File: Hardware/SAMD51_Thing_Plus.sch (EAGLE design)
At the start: 52 parts, among them Q1 2.5A/30V, Q2 MBT3904DW1T1, U1 MCP73831, U2 ESP-WROOM-32, U3 AP2112K-3.3V, U4 FT231XS

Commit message: First commit for samd51
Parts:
- removed C16: 0.1uF, SparkFun-Capacitors:0.1UF-0603-25V-(+80/-20%)
- removed Q2: MBT3904DW1T1, esp32-thing-temp:MBT3904DW1T1
- removed R10, R17, R18, R2: 10k, SparkFun-Resistors:10KOHM-0603-1/10W-1%
- removed R13, R14: 27, SparkFun-Resistors:27OHM1/10W1%(0603)0603-RES
- removed R9: 10k, SparkFun-Resistors:10KOHM-1/10W-1%(0603)0603
- removed S2: BTN-0, SparkFun-Electromechanical:SWITCH-MOMENTARY-2SMD-4.6X2.8MM
- added C4, C8, C9: 0.1uF, SparkFun-Capacitors:0.1UF-0402-16V-10%
- added C5: 10uF, SparkFun-Capacitors:10UF-0603-6.3V-20%
- added FD3, FD4: FIDUCIALUFIDUCIAL, SparkFun-Aesthetics:FIDUCIALUFIDUCIAL
- added J4: CORTEX_DEBUG_PTH, SparkFun-Connectors:CORTEX_DEBUG_PTH
- added J5: 455-1750-1-ND, SparkFun-Connectors:CONN_03
- added L1: FB - 30Ohm, SparkFun-Passives:INDUCTOR0603
- added R1: 10k, SparkFun-Resistors:10KOHM-0603-1/10W-1%
- added Y1: 32.768kHz, SparkFun-Clocks:CRYSTAL-32.768KHZSMD-3.2X1.5
- C1: value 0.1uF -> 15pF; device SparkFun-Capacitors:0.1UF-0603-25V-5% -> SparkFun-Capacitors:15PF-0402-50V-5%
- C11, C14: device SparkFun-Capacitors:0.1UF-0603-25V-(+80/-20%) -> SparkFun-Capacitors:0.1UF-0402-16V-10%
- C12: value 47pF -> 0.1uF; device SparkFun-Capacitors:47PF-0603-50V-5% -> SparkFun-Capacitors:0.1UF-0402-16V-10%
- C13: value 47pF -> 4.7uF; device SparkFun-Capacitors:47PF-0603-50V-5% -> SparkFun-Capacitors:4.7UF0603
- C15: value 4.7uF -> 10uF; device SparkFun-Capacitors:4.7UF-6.3V-10%(0603)0603 -> SparkFun-Capacitors:10UF-0805-10V-10%
- C2: value 10uF -> 15pF; device SparkFun-Capacitors:10UF-0805-10V-10% -> SparkFun-Capacitors:15PF-0402-50V-5%
- C3: device SparkFun-Capacitors:0.1UF-0603-25V-5% -> SparkFun-Capacitors:0.1UF-0402-16V-10%
- LOGO1: value SFE_LOGO_NAME.1_INCH -> SFE_LOGO_NAME_FLAME.2_INCH; device SparkFun-Aesthetics:SFE_LOGO_NAME.1_INCH -> SparkFun-Aesthetics:SFE_LOGO_NAME_FLAME.2_INCH
- U2: value ESP-WROOM-32 -> ATSAMD51J20A-A; device SparkFun-RF:ESP-WROOM-32 -> SparkFun-IC-Microcontroller:ATSAMD51J20A-A
- U4: value FT231XS -> RFM69HW; device SparkFun-DigitalIC:FT231XS -> SparkFun-RF:RFM69HW
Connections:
- removed net 3.3V_F: C16.1, U4.!RESET, U4.3V3OUT, U4.VCCIO
- removed net CHIP_PU: C3.1, J1.6, Q2Q1.C, R2.1, S1.2, U2.EN
- removed net DTR: Q2Q2.E, R17.1, U4.!DTR
- removed net N$10: Q2Q1.B, R17.2
- removed net N$12: Q2Q2.B, R18.2
- removed net N$7: R13.2, U4.USBDM
- removed net N$8: R14.2, U4.USBDP
- removed net RTS: Q2Q1.E, R18.1, U4.!RTS
- new net !RESET: J1.6, J4.!RESET, R1.1, S1.2, U2.!RESET
- new net N$4: J5.2, U4.ANT
- new net RFM_MISO: U2.PA19, U4.MISO
- new net RFM_MOSI: U2.PA16, U4.MOSI
- new net RFM_RESET: U2.PA20, U4.RESET
- new net RFM_SCK: U2.PA17, U4.SCK
- new net RFM_SS: U2.PA18, U4.NSS
- new net SWDCLK: J4.SWDCLK/TCK, U2.PA30
- new net SWDIO: J4.SWDIO/TMS, U2.PA31
- new net VCC: C13.1, C14.1, U2.VDDCORE
- new net VDDA: C12.1, C15.1, L1.2, U2.PA03, U2.VDDANA
- new net XIN32: C1.1, U2.PA00, Y1.1
- new net XOUT32: C2.1, U2.PA01, Y1.2
- net 0: now also U2.PA13; no longer Q2Q2.C, R9.1, S2.2, U2.IO0
- net 12: now also U2.PA07; no longer R10.2, U2.IO12
- net 13: now also U2.PA10; no longer U2.IO13
- net 14: now also U2.PA06; no longer U2.IO14
- net 15: now also U2.PA11; no longer U2.IO15
- net 16: now also U2.PA09; no longer U2.IO16
- net 17: now also U2.PA08; no longer U2.IO17
- net 18: now also U2.PB13; no longer U2.IO18
- net 19: now also U2.PB15; no longer U2.IO19
- net 2: now also U2.PB14; no longer U2.IO2
- net 20: now also U2.PA12; no longer U2.IO20
- net 21: now also U2.PB16; no longer U2.IO21
- net 22: now also U2.PB17; no longer U2.IO22
- net 23: now also U2.PB12; no longer U2.IO23
- net 25: now also U2.PA02; no longer U2.IO25
- net 26: now also U2.PA05; no longer U2.IO26
- net 27: now also U2.PA04; no longer U2.IO27
- net 3.3V: now also C11.1, C3.1, C4.1, C5.1, C8.1, C9.1, J4.VCC, L1.1, R1.2, U2.VDDIO0, U2.VDDIO1, U2.VDDIO2, U2.VDDIO3, U4.3.3V; no longer C1.1, C2.1, R2.2, R9.2, U2.3V3
- net 32: now also U2.PB08; no longer U2.IO32
- net 33: now also U2.PB09; no longer U2.IO33
- net 34: now also U2.PB02; no longer U2.IO34
- net 35: now also U2.PB03; no longer U2.IO35
- net 4: now also U2.PA14; no longer U2.IO4
- net 5: now also U2.PA15; no longer U2.IO5
- net D+: now also U2.PA25; no longer C13.1, R14.1
- net D-: now also U2.PA24; no longer C12.1, R13.1
- net GND: now also C4.2, C5.2, C8.2, C9.2, J4.GND@3, J4.GND@5, J5.1, J5.3, U2.GND0, U2.GND1, U2.GND2, U2.GND3, U2.GND4, U4.GND@1, U4.GND@2; no longer C16.2, R10.1, S2.1, U2.GND, U2.GND@1, U2.GND@15, U2.GND@38, U4.GND@16, U4.GND@6
- net U0RXD: now also U2.PB31; no longer U2.RXD, U4.TXD
- net U0TXD: now also U2.PB30; no longer U2.TXD, U4.RXD
- net VUSB-RAW: no longer C11.1
- net V_USB: no longer C14.1, C15.1, U4.VCC
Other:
- note added: "01"
- note added: "C11 to be near U2.56"
- note added: "C12 to be near U2.8"
- note added: "C13 & C14 to be near U2.53"
- note added: "C3 to be near U2.48"
- note added: "C8 to be near U2.21"
- note added: "C9 to be near U2.34"
- note added: "MISO"
- note added: "MOSI"
- note added: "Original ESP32 Thing by Jim Lindblom ESP32 Thing Plus by Mike Hord"
- note added: "SCK"
- note added: "SERCOM0 for UART2"
- note added: "SERCOM1 for RFM"
- note added: "SERCOM4 for SPI"
- note added: "SERCOM5 for I2C"
- note added: "SERCOM7 for UART0"
- note added: "SS"
- note removed: "Auto-Reset"
- note removed: "Boot Mode Configuration Pin Default Boot Download GPIO0 1 1 0 U0TXD 1 1 x GPIO2 0 x 0 GPIO4 0 x x MTDO 1 x x GPIO5 1 1 x If U0TXD, GPIO2, GPIO5 are floating, GPIO0 determines boot mode"
- note removed: "GPIO0 Button"
- note removed: "If DTR is LOW, toggling RTS from HIGH to LOW resets to run mode. If RTS is HIGH, toggling DTR from LOW to HIGH resets to bootloader."
- note removed: "Jim Lindblom"
- note removed: "v10"
- moved on the sheet: C1, C11, C12, C13, C14, C15, C2, C3

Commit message: Post review feedback and engineer checklist
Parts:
- removed JP15: (no value), SparkFun-Connectors:USB_MICROB_PLUGCONN-11752
- added J6: (no value), SparkFun-Connectors:USB_MICRO-B_HALF_PTH_2
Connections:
- removed net SHIELD: JP15.SHIELD
- net D+: now also J6.D+; no longer JP15.D+
- net D-: now also J6.D-; no longer JP15.D-
- net GND: now also J6.GND; no longer JP15.GND
- net VUSB-RAW: now also J6.VBUS; no longer JP15.VCC
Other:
- note added: "Mike Hord"
- note added: "Original ESP32 Thing by Jim Lindblom"
- note added: "QWIIC Connector"
- note added: "RFM69"
- note added: "SAMD51"
- note added: "SWD Programming Header"
- note added: "USB Connector"
- note removed: "Espressif ESP32"
- note removed: "FT231XS (USB-to-Serial Converter)"
- note removed: "Original ESP32 Thing by Jim Lindblom ESP32 Thing Plus by Mike Hord"
- moved on the sheet: F1, J3, J4, J5, R1, U2, U4

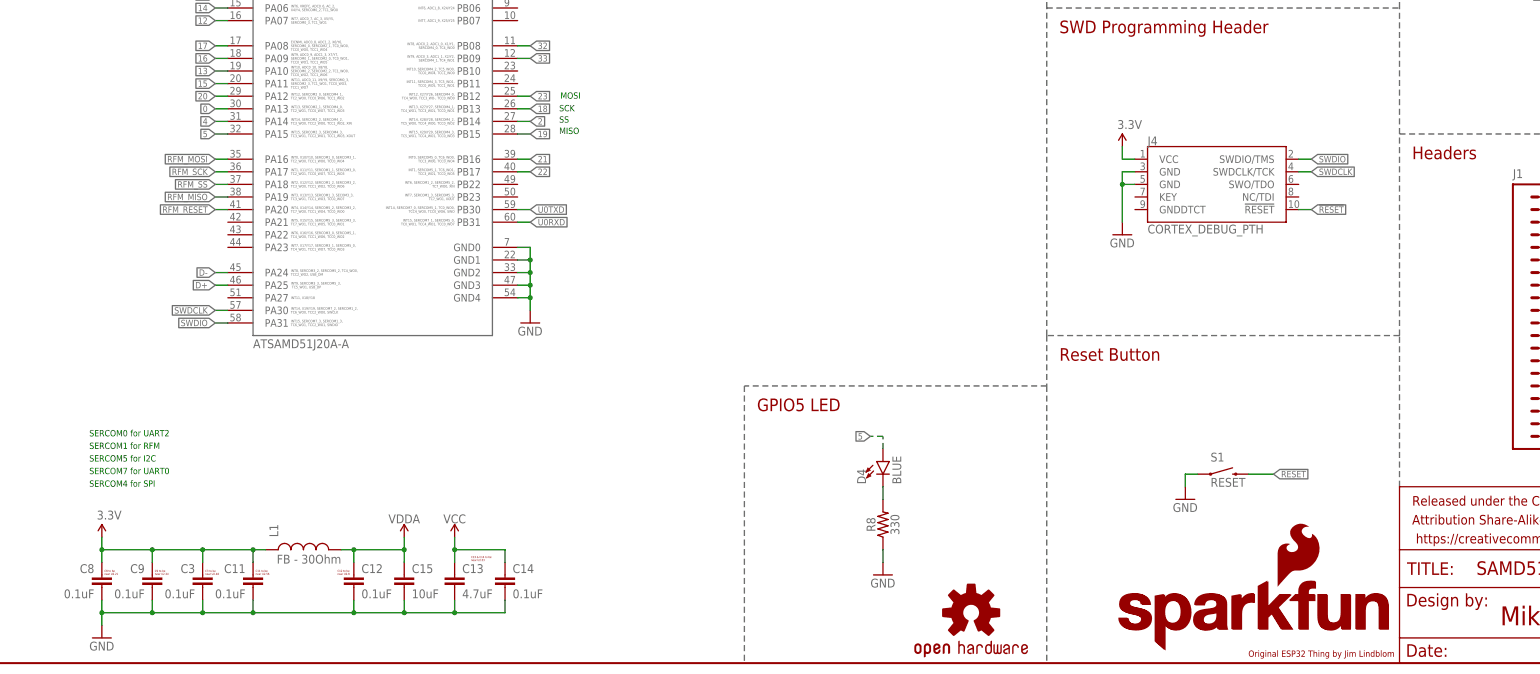
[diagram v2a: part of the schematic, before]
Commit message: Fixes from QC review
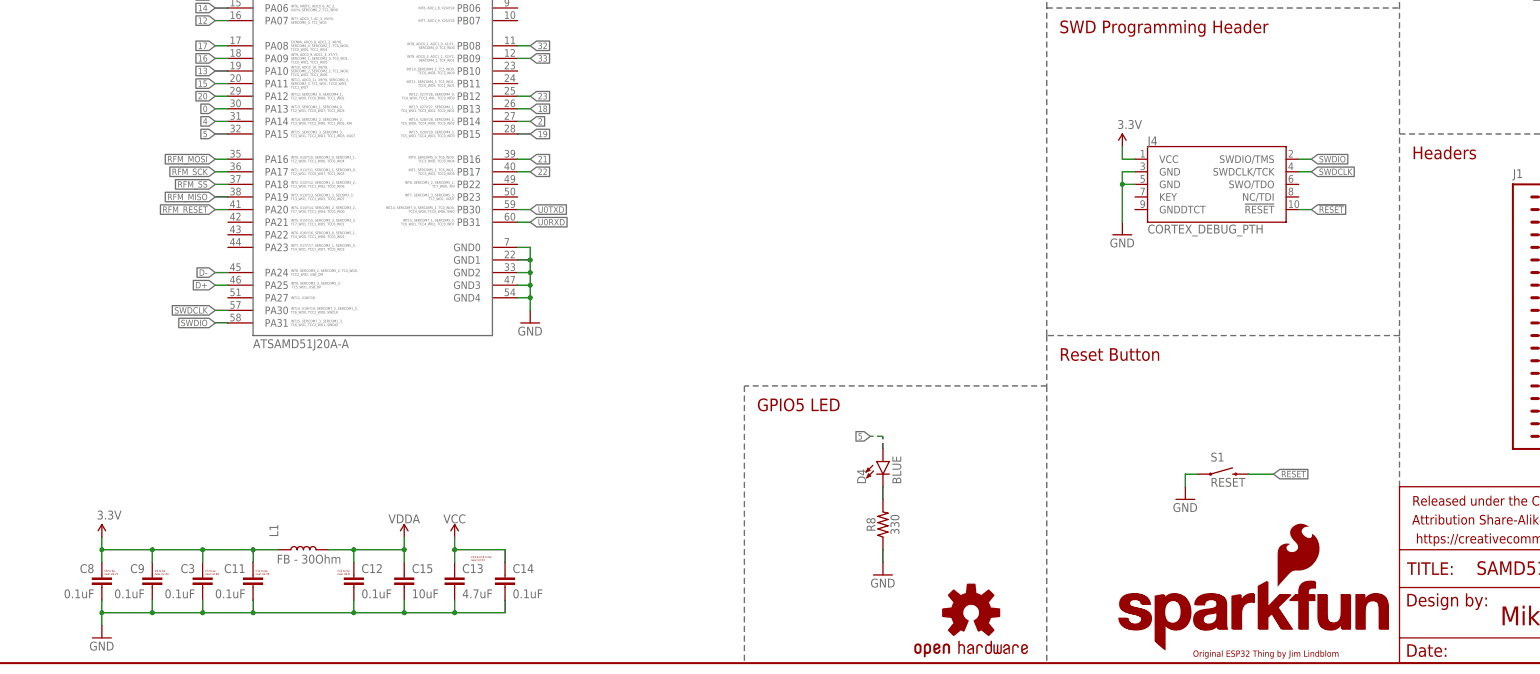
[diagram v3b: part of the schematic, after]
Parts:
- J6: device SparkFun-Connectors:USB_MICRO-B_HALF_PTH_2 -> SparkFun-Connectors:USB_MICRO-B_HALF_PTH_MILL
- L1: device SparkFun-Passives:INDUCTOR0603 -> SparkFun-Coils:INDUCTORFB-30OHM; PROD_ID RES-07859 -> NDUC-07859
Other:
- note removed: "MISO"
- note removed: "MOSI"
- note removed: "SCK"
- note removed: "SERCOM0 for UART2"
- note removed: "SERCOM1 for RFM"
- note removed: "SERCOM4 for SPI"
- note removed: "SERCOM5 for I2C"
- note removed: "SERCOM7 for UART0"
- note removed: "SS"

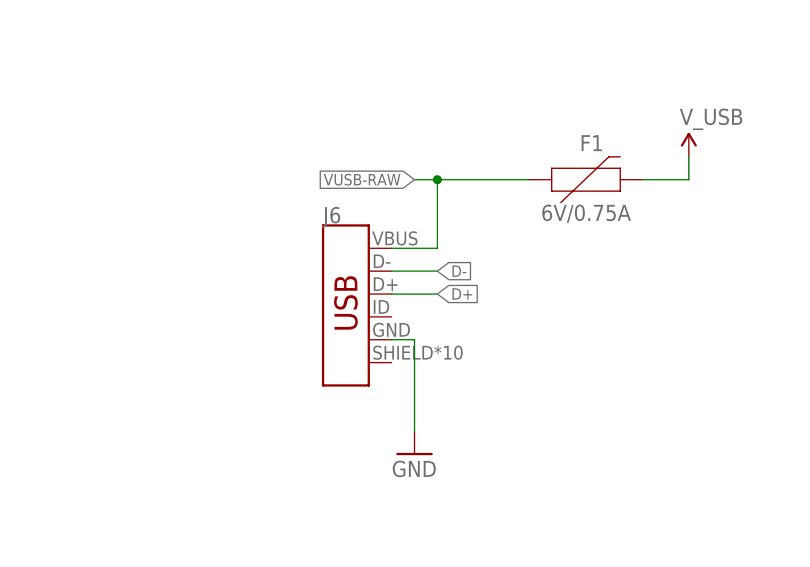
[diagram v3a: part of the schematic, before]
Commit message: Replaced retired 1.0uF cap with new one
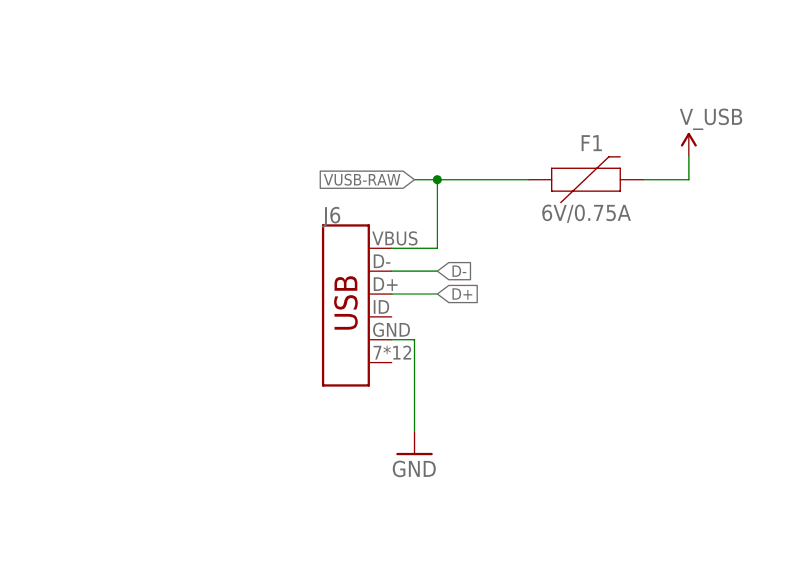
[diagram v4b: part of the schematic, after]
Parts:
- C7: device SparkFun-Capacitors:1.0UF-0805-25V-(+80/-20%) -> SparkFun-Capacitors:1.0UF-0603-16V-10%-X7R
- J6: value (none) -> AMP FCI 10103594-0001LF; device SparkFun-Connectors:USB_MICRO-B_HALF_PTH_MILL -> SparkFun-Connectors:USB_MICRO-B_HALF_PTH
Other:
- moved on the sheet: J6
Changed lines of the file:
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@@
 <part name="F1" library="SparkFun-Fuses" deviceset="PPTC" device="_THREE-QUARTER-AMP" value="6V/0.75A"/>
 <part name="GND15" library="SparkFun-Aesthetics" deviceset="GND" device=""/>
-<part name="C7" library="SparkFun-Capacitors" deviceset="1.0UF" device="-0805-25V-(+80/-20%)" value="1.0uF"/>
+<part name="C7" library="SparkFun-Capacitors" deviceset="1.0UF" device="-0603-16V-10%-X7R" value="1.0uF"/>
 <part name="C10" library="SparkFun-Capacitors" deviceset="2.2UF" device="-0603-10V-20%" value="2.2uF"/>
 <part name="GND21" library="SparkFun-Aesthetics" deviceset="GND" device=""/>
@@
 <part name="GND8" library="SparkFun-Aesthetics" deviceset="GND" device=""/>
 <part name="LOGO1" library="SparkFun-Aesthetics" deviceset="SFE_LOGO_NAME_FLAME" device=".2_INCH"/>
-<part name="J6" library="SparkFun-Connectors" deviceset="USB_MICRO-B" device="_HALF_PTH_MILL"/>
+<part name="J6" library="SparkFun-Connectors" deviceset="USB_MICRO-B" device="_HALF_PTH" value="AMP FCI 10103594-0001LF"/>
 </parts>
 <sheets>
@@
 <instance part="GND8" gate="1" x="10.16" y="127"/>
 <instance part="LOGO1" gate="G$1" x="272.796" y="2.286"/>
-<instance part="J6" gate="J1" x="330.2" y="233.68"/>
+<instance part="J6" gate="J1" x="330.2" y="233.68" smashed="yes">
+<attribute name="NAME" x="327.66" y="244.094" size="1.778" layer="95" font="vector"/>
+</instance>
 </instances>
 <busses>

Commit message: Buzzard Text
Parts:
- removed C4: 0.1uF, SparkFun-Capacitors:0.1UF-0402-16V-10%
- removed C5: 10uF, SparkFun-Capacitors:10UF-0603-6.3V-20%
- removed D3: RED, SparkFun-LED:LED-RED0603
- removed F1: 6V/0.75A, SparkFun-Fuses:PPTC_THREE-QUARTER-AMP
- removed J4: CORTEX_DEBUG_PTH, SparkFun-Connectors:CORTEX_DEBUG_PTH
- removed J5: 455-1750-1-ND, SparkFun-Connectors:CONN_03
- removed LOGO1: SFE_LOGO_NAME_FLAME.2_INCH, SparkFun-Aesthetics:SFE_LOGO_NAME_FLAME.2_INCH
- removed LOGO3: SFE_LOGO_NAME.2_INCH, SparkFun-Aesthetics:SFE_LOGO_NAME.2_INCH
- removed R5: DNP, SparkFun-Passives:RESISTORPTH-1/6W
- removed SJ1, SJ2: JUMPER-PAD-2-NC_BY_TRACE, SparkFun-Passives:JUMPER-PAD-2-NC_BY_TRACE
- added R2: 10k, SparkFun-Resistors:10KOHM-0603-1/10W-1%
- added TP1, TP2: TEST-POINTTP_15TH_THRU, SparkFun-Connectors:TEST-POINTTP_15TH_THRU
- J1: device SparkFun-Connectors:M20NOSILK -> SparkFun-Connectors:CONN_12NO_SILK
- J2: device SparkFun-Connectors:M20NOSILK -> SparkFun-Connectors:CONN_161X16_NO_SILK
- JP2: device SparkFun-Connectors:M02JST-PTH-2 -> SparkFun-Connectors:CONN_02-JST-2MM-SMT
- R4: value 1K -> 10k; device SparkFun-Resistors:1KOHM-1/10W-1%(0603) -> SparkFun-Resistors:10KOHM-0603-1/10W-1%
- S1: device SparkFun-Electromechanical:SWITCH-MOMENTARY-2SMD-4.6X2.8MM -> SparkFun-Switches:MOMENTARY-SWITCH-SPST-2-SMD-4.6X2.8MM
- U4: value RFM69HW -> 4MB Flash; device SparkFun-RF:RFM69HW -> SparkFun-IC-Memory:AT25SF041
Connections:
- removed net 0: J2.7, U2.PA13
- removed net 12: J1.12, U2.PA07
- removed net 13: J1.11, U2.PA10
- removed net 14: J1.13, U2.PA06
- removed net 15: J1.10, U2.PA11
- removed net 16: J2.9, U2.PA09
- removed net 17: J2.10, U2.PA08
- removed net 18: J2.12, U2.PB13
- removed net 19: J2.13, U2.PB15
- removed net 2: J2.6, U2.PB14
- removed net 20: J2.14, U2.PA12
- removed net 21: J2.15, J3.3, U2.PB16
- removed net 22: J2.18, J3.4, U2.PB17
- removed net 23: J2.19, U2.PB12
- removed net 25: J1.16, U2.PA02
- removed net 26: J1.15, U2.PA05
- removed net 27: J1.14, U2.PA04
- removed net 32: J1.18, U2.PB08
- removed net 33: J1.17, U2.PB09
- removed net 34: J1.20, U2.PB02
- removed net 35: J1.19, U2.PB03
- removed net 4: J2.8, U2.PA14
- removed net 5: D4.A, J2.11, U2.PA15
- removed net N$16: R6.2, SJ1.1
- removed net N$2: D3.A, R4.2
- removed net N$3: R4.1, SJ2.1
- removed net N$4: J5.2, U4.ANT
- removed net RFM_MISO: U2.PA19, U4.MISO
- removed net RFM_MOSI: U2.PA16, U4.MOSI
- removed net RFM_RESET: U2.PA20, U4.RESET
- removed net RFM_SCK: U2.PA17, U4.SCK
- removed net RFM_SS: U2.PA18, U4.NSS
- removed net U0RXD: J2.16, U2.PB31
- removed net U0TXD: J2.17, U2.PB30
- removed net VUSB-RAW: F1.1, J1.2, J2.2, J6.VBUS
- new net A0: J2.5, U2.PA02
- new net A1: J2.6, U2.PB08
- new net A2: J2.7, U2.PB09
- new net A3: J2.8, U2.PA04
- new net A4: J2.9, U2.PA05
- new net A5: J2.10, U2.PB02
- new net D0: J2.14, U2.PA11
- new net D1: J2.15, U2.PA10
- new net D10: J1.7, U2.PA18
- new net D11: J1.6, U2.PA16
- new net D12: J1.5, U2.PA19
- new net D13: D4.A, J1.4, U2.PA17
- new net D2_FLASH_MISO: U2.PA14
- new net D3_FLASH_SCK: U2.PA09
- new net D4_FLASH_MOSI: U2.PA08
- new net D5: J1.10, U2.PA15
- new net D6: J1.9, U2.PA20
- new net D7: U2.PA21
- new net D8: U2.PA06
- new net D9: J1.8, U2.PA07
- new net EN: J1.2, R2.1, U3.EN
- new net FLASH_CS: R4.1, U2.PA13, U4.!CS
- new net MISO: J2.13, U2.PA12
- new net MOSI: J2.12, U2.PB10
- new net RXD: U2.PB23
- new net RXLED: U2.PB03
- new net SCK: J2.11, U2.PB11
- new net SCL: J1.11, J3.4, U2.PA23
- new net SDA: J1.12, J3.3, U2.PA22
- new net TXD: U2.PB22
- new net TXLED: U2.PA27
- net !RESET: now also J2.1, S1.4; no longer J1.6, J4.!RESET, S1.2
- net 3.3V: now also J2.2, R4.2, U4.VCC; no longer C4.1, C5.1, J1.5, J2.5, J4.VCC, SJ2.2, U4.3.3V
- net GND: now also J2.16; no longer C4.2, C5.2, D3.C, J1.1, J1.4, J1.7, J1.8, J1.9, J2.1, J2.20, J4.GND@3, J4.GND@5, J5.1, J5.3, R5.1, U4.GND@1, U4.GND@2
- net N$14: now also R6.2; no longer R5.2, SJ1.2
- net SWDCLK: now also TP2.1; no longer J4.SWDCLK/TCK
- net SWDIO: now also TP1.1; no longer J4.SWDIO/TMS
- net VIN: now also R2.2; no longer U3.EN
- net V_BATT: now also J1.1; no longer J1.3, J2.3
- net V_USB: now also J1.3, J6.VBUS; no longer F1.2
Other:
- note removed: "RFM69"
- note removed: "SJ1 can be cut to modify the charge- current programming resistor."
- note removed: "SJ2 disconnects the power LED (for power saving)."
- note removed: "SWD Programming Header"
- moved on the sheet: C10, R4, U3
